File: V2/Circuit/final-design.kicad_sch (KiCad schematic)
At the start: 27 parts, among them J1 Conn_02x05_Odd_Even, U1 LM338T, U2 TMC2209_SILENTSTEPSTICK

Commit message: minor changes in circuit and more dev in programming
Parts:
- renumbered StopButton1 to ControlSwitch1, ControlSwitch1 to StopButton1
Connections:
- net STOP_Button: now also MCU1.21 (CMP-/RxD_2/INT2/P3.6), StopButton1.1 (Pin_1); no longer ControlSwitch1.1 (Pin_1), MCU1.19 (COMO/PWM8_2/PWM4P_4/MOSI_4/T1CLKO/T0/P3.4)
- net control-mode-switch: now also ControlSwitch1.1 (Pin_1), MCU1.19 (COMO/PWM8_2/PWM4P_4/MOSI_4/T1CLKO/T0/P3.4); no longer MCU1.21 (CMP-/RxD_2/INT2/P3.6), StopButton1.1 (Pin_1)
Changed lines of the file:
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@@
 	(global_label "control-mode-switch"
 		(shape input)
-		(at 77.47 151.13 0)
+		(at 77.47 97.79 0)
 		(fields_autoplaced yes)
 		(effects
@@
 		)
 		(property "Intersheetrefs" "${INTERSHEET_REFS}"
-			(at 101.3193 151.13 0)
+			(at 101.3193 97.79 0)
 			(effects
 				(font
@@
 	(global_label "control-mode-switch"
 		(shape input)
-		(at 191.77 39.37 0)
+		(at 191.77 44.45 0)
 		(fields_autoplaced yes)
 		(effects
@@
 		)
 		(property "Intersheetrefs" "${INTERSHEET_REFS}"
-			(at 215.6193 39.37 0)
+			(at 215.6193 44.45 0)
 			(effects
 				(font
@@
 	(global_label "STOP_Button"
 		(shape input)
-		(at 191.77 44.45 0)
+		(at 191.77 39.37 0)
 		(fields_autoplaced yes)
 		(effects
@@
 		)
 		(property "Intersheetrefs" "${INTERSHEET_REFS}"
-			(at 206.6688 44.45 0)
+			(at 206.6688 39.37 0)
 			(effects
 				(font
@@
 	(global_label "STOP_Button"
 		(shape input)
-		(at 77.47 97.79 0)
+		(at 77.47 151.13 0)
 		(fields_autoplaced yes)
 		(effects
@@
 		)
 		(property "Intersheetrefs" "${INTERSHEET_REFS}"
-			(at 92.3688 97.79 0)
+			(at 92.3688 151.13 0)
 			(effects
 				(font
@@
 		(on_board yes)
 		(dnp no)
-		(property "Reference" "StopButton1"
+		(property "Reference" "ControlSwitch1"
 			(at 72.39 106.68 0)
 			(effects
@@
 			(project "final-design"
 				(path "/90fcdb5f-e6ac-4407-b69d-2c32848d2af5"
-					(reference "StopButton1")
+					(reference "ControlSwitch1")
 					(unit 1)
 				)
@@
 		(on_board yes)
 		(dnp no)
-		(property "Reference" "ControlSwitch1"
+		(property "Reference" "StopButton1"
 			(at 72.39 160.02 0)
 			(effects
@@
 			(project "final-design"
 				(path "/90fcdb5f-e6ac-4407-b69d-2c32848d2af5"
-					(reference "ControlSwitch1")
+					(reference "StopButton1")
 					(unit 1)
 				)

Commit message: minor circuit changes
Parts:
- R4: value 200 -> 150
- R5: value 330 -> 470
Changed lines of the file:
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@@
 	(label "PSB"
 		(at 180.34 142.24 0)
-		(fields_autoplaced yes)
 		(effects
 			(font
@@
 	(label "VO"
 		(at 185.42 139.7 180)
-		(fields_autoplaced yes)
 		(effects
 			(font
@@
 	(label "TX"
 		(at 199.39 54.61 0)
-		(fields_autoplaced yes)
 		(effects
 			(font
@@
 	(label "RX"
 		(at 199.39 52.07 0)
-		(fields_autoplaced yes)
 		(effects
 			(font
@@
 			)
 		)
-		(property "Value" "330"
+		(property "Value" "470"
 			(at 149.86 90.17 90)
 			(effects
@@
 			)
 		)
-		(property "Value" "200"
+		(property "Value" "150"
 			(at 149.86 80.01 90)
 			(effects

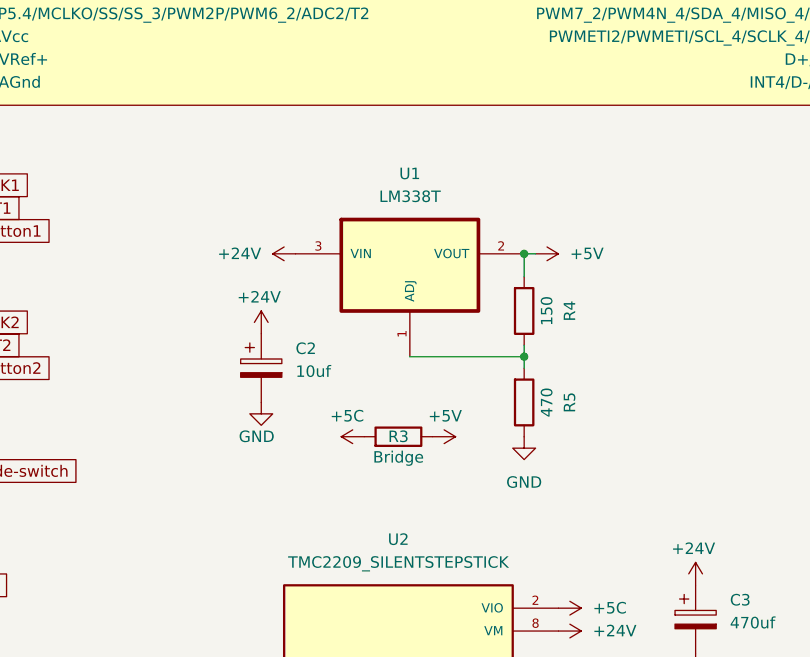
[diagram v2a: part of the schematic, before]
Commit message: upgraded board to use l7805 instead of lm317
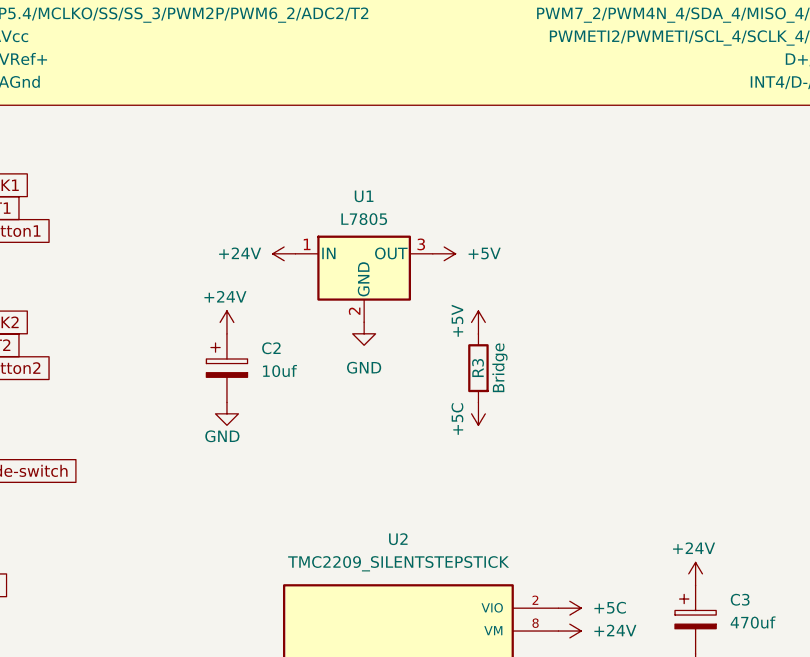
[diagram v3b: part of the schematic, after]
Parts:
- removed R4: 150, Resistor_THT:R_Axial_DIN0207_L6.3mm_D2.5mm_P7.62mm_Horizontal, symbol Device:R
- removed R5: 470, Resistor_THT:R_Axial_DIN0207_L6.3mm_D2.5mm_P7.62mm_Horizontal, symbol Device:R
- removed U1: LM338T, LM338T:TO254P1054X470X1955-3, symbol LM338T:LM338T
- added U1: L7805, Package_TO_SOT_THT:TO-220-3_Vertical, symbol Regulator_Linear:L7805
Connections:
- net +24V: now also U1.1 (IN)
- net +5V: now also U1.3 (OUT)
- net GND: now also U1.2 (GND)
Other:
- moved on the sheet: C2, R3
